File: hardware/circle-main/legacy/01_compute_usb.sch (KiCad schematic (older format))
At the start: 10 parts, among them J1 USB-C-USB2, U1 ESP32-S3-WROOM-1-N16R8, U6 MCP23017

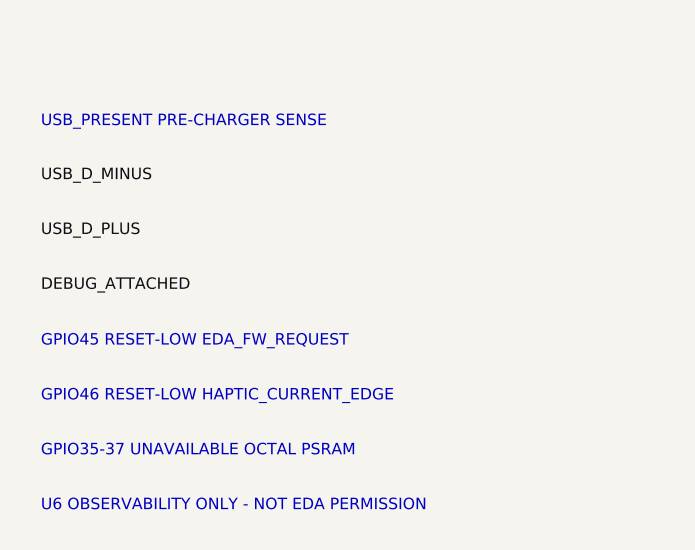
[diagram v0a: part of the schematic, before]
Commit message: Make every CIRCLE review claim reproducible
Validate and export the architecture-level schematics with KiCad 10.0.5, add zero-violation ERC gates, engineering documentation, and one-command evidence hashing.

Constraint: KiCad CLI does not import legacy .sch into native .kicad_sch

Rejected: Hand-written native S-expressions | would create unvalidated CAD

Confidence: medium

Scope-risk: broad

Reversibility: clean

Directive: Treat NET annotations as architecture interfaces, not fabrication-ready connectivity

Tested: py -3.11 tools/verify_release.py; 30 tests; KiCad 10.0.5 ERC/BOM/PDF/SVG/netlist exports

Not-tested: Native conversion, PCB layout, footprints, powered electrodes, human connection, EMC, or regulatory compliance
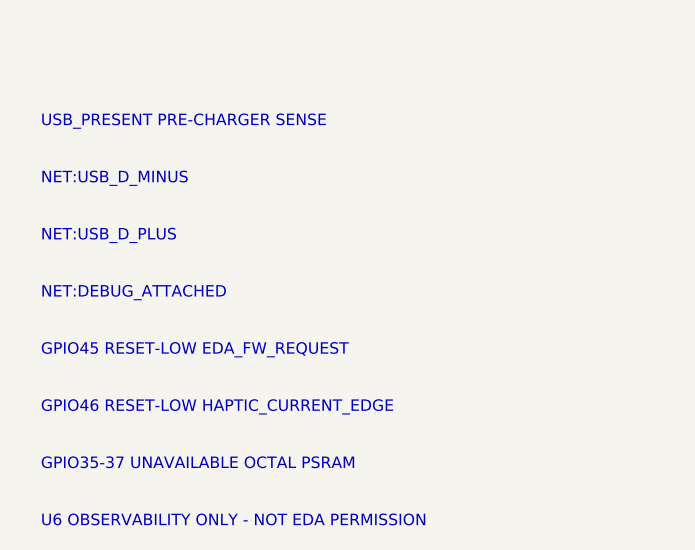
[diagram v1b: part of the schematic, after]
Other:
- note added: "NET:DEBUG_ATTACHED"
- note added: "NET:USB_D_MINUS"
- note added: "NET:USB_D_PLUS"
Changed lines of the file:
@@
 Sheet 1 1
 Title "ESP32-S3 compute and USB"
+Date "2026-08-14"
+Rev "A"
+Comp "Vers3Dynamics"
 Comment1 "ENGINEERING REVIEW ONLY - NOT FOR HUMAN CONNECTION"
+Comment2 "Generated artifact - edit manifest/generator"
+Comment3 ""
+Comment4 ""
 $EndDescr
 $Comp
@@
 F 0 "U1" H 1400 1300 50  0000 C CNN
 F 1 "ESP32-S3-WROOM-1-N16R8" H 1400 1100 50  0000 C CNN
+F 2 "" H 1300 1200 50  0001 C CNN
+F 3 "" H 1300 1200 50  0001 C CNN
+	1    1300 1200
 	1    0    0    -1
 $EndComp
@@
 F 0 "J1" H 3500 1300 50  0000 C CNN
 F 1 "USB-C-USB2" H 3500 1100 50  0000 C CNN
+F 2 "" H 3400 1200 50  0001 C CNN
+F 3 "" H 3400 1200 50  0001 C CNN
+	1    3400 1200
 	1    0    0    -1
 $EndComp
@@
 F 0 "D1" H 5600 1300 50  0000 C CNN
 F 1 "TPD4E05U06" H 5600 1100 50  0000 C CNN
+F 2 "" H 5500 1200 50  0001 C CNN
+F 3 "" H 5500 1200 50  0001 C CNN
+	1    5500 1200
 	1    0    0    -1
 $EndComp
@@
 F 0 "R1" H 7700 1300 50  0000 C CNN
 F 1 "5.1k" H 7700 1100 50  0000 C CNN
+F 2 "" H 7600 1200 50  0001 C CNN
+F 3 "" H 7600 1200 50  0001 C CNN
+	1    7600 1200
 	1    0    0    -1
 $EndComp
@@
 F 0 "R2" H 1400 2100 50  0000 C CNN
 F 1 "5.1k" H 1400 1900 50  0000 C CNN
+F 2 "" H 1300 2000 50  0001 C CNN
+F 3 "" H 1300 2000 50  0001 C CNN
+	1    1300 2000
 	1    0    0    -1
 $EndComp
@@
 F 0 "R3" H 3500 2100 50  0000 C CNN
 F 1 "22R" H 3500 1900 50  0000 C CNN
+F 2 "" H 3400 2000 50  0001 C CNN
+F 3 "" H 3400 2000 50  0001 C CNN
+	1    3400 2000
 	1    0    0    -1
 $EndComp
@@
 F 0 "R4" H 5600 2100 50  0000 C CNN
 F 1 "22R" H 5600 1900 50  0000 C CNN
+F 2 "" H 5500 2000 50  0001 C CNN
+F 3 "" H 5500 2000 50  0001 C CNN
+	1    5500 2000
 	1    0    0    -1
 $EndComp
@@
 F 0 "S1" H 7700 2100 50  0000 C CNN
 F 1 "BOOT" H 7700 1900 50  0000 C CNN
+F 2 "" H 7600 2000 50  0001 C CNN
+F 3 "" H 7600 2000 50  0001 C CNN
+	1    7600 2000
 	1    0    0    -1
 $EndComp
@@
 F 0 "S2" H 1400 2900 50  0000 C CNN
 F 1 "RESET" H 1400 2700 50  0000 C CNN
+F 2 "" H 1300 2800 50  0001 C CNN
+F 3 "" H 1300 2800 50  0001 C CNN
+	1    1300 2800
 	1    0    0    -1
 $EndComp
@@
 F 0 "U6" H 3500 2900 50  0000 C CNN
 F 1 "MCP23017" H 3500 2700 50  0000 C CNN
+F 2 "" H 3400 2800 50  0001 C CNN
+F 3 "" H 3400 2800 50  0001 C CNN
+	1    3400 2800
 	1    0    0    -1
 $EndComp
-Text Label 700 5840 0    50   ~ 0
-USB_D_MINUS
-Text Label 700 6080 0    50   ~ 0
-USB_D_PLUS
-Text Label 700 6320 0    50   ~ 0
-DEBUG_ATTACHED
 Text Notes 600 400 0    50   ~ 0
 ENGINEERING REVIEW ONLY - NOT FOR HUMAN CONNECTION
 Text Notes 700 5600 0    50   ~ 0
 USB_PRESENT PRE-CHARGER SENSE
-Text Notes 700 6560 0    50   ~ 0
+Text Notes 700 5850 0    50   ~ 0
+NET:USB_D_MINUS
+Text Notes 700 6100 0    50   ~ 0
+NET:USB_D_PLUS
+Text Notes 700 6350 0    50   ~ 0
+NET:DEBUG_ATTACHED
+Text Notes 700 6600 0    50   ~ 0
 GPIO45 RESET-LOW EDA_FW_REQUEST
-Text Notes 700 6800 0    50   ~ 0
+Text Notes 700 6850 0    50   ~ 0
 GPIO46 RESET-LOW HAPTIC_CURRENT_EDGE
-Text Notes 700 7040 0    50   ~ 0
+Text Notes 700 7100 0    50   ~ 0
 GPIO35-37 UNAVAILABLE OCTAL PSRAM
-Text Notes 700 7280 0    50   ~ 0
+Text Notes 700 7350 0    50   ~ 0
 U6 OBSERVABILITY ONLY - NOT EDA PERMISSION
 $EndSCHEMATC
